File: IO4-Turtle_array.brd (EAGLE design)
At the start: 106 x 106 mm, 61 parts

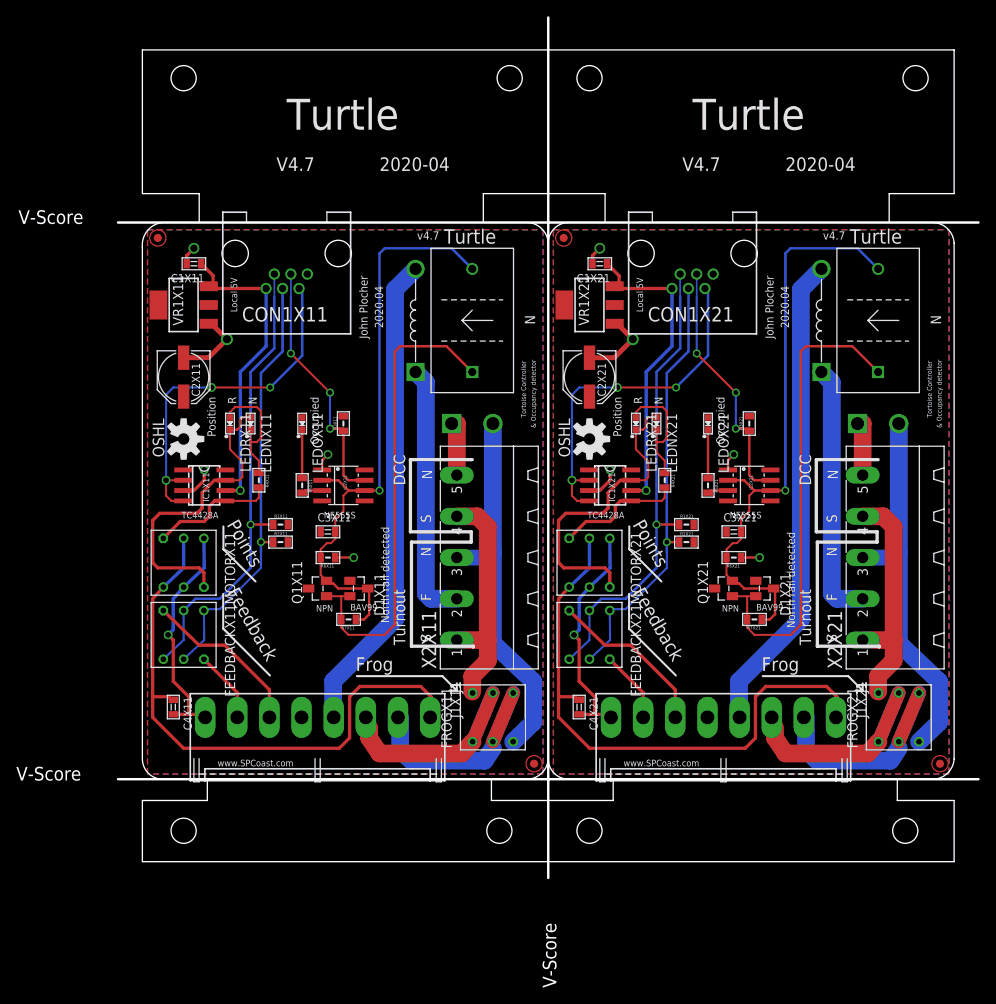
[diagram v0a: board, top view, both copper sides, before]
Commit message: silkscreen cleanup, better power routing
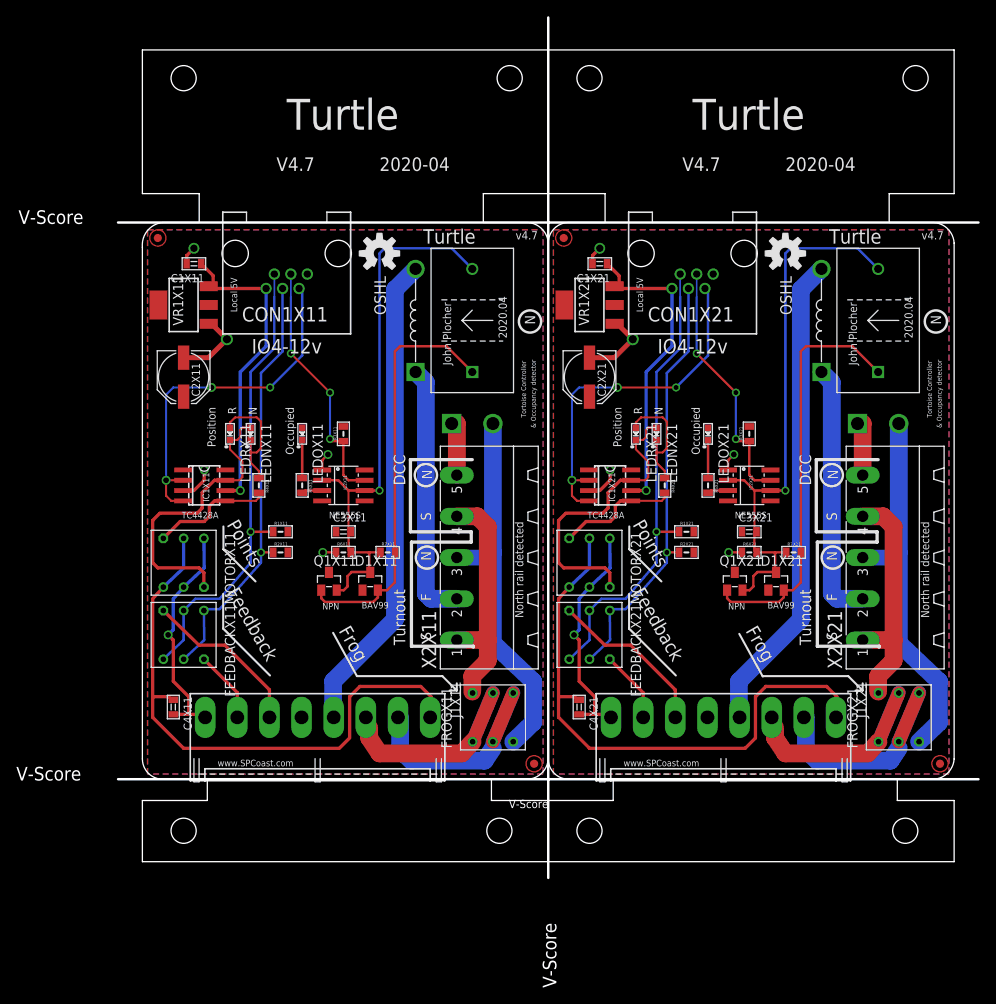
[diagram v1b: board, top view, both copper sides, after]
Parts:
- moved OSHW1X11 33.2 mm to (29.2, 74.9), turned to 0 degrees
- moved OSHW1X21 33.2 mm to (79.2, 74.9), turned to 0 degrees
- moved R7X11 9.56 mm to (30.2, 38.1), turned to 0 degrees
- moved R7X21 9.56 mm to (80.2, 38.1), turned to 0 degrees
- moved R6X11 2.01 mm to (24.8, 38.1), turned to 0 degrees
- moved R6X21 2.01 mm to (74.8, 38.1), turned to 0 degrees
- moved C3X11 1.91 mm to (24.8, 40.6)
- moved C3X21 1.91 mm to (74.8, 40.6)
- moved D1X11 1.66 mm to (28.1, 34.5), turned to 0 degrees
- moved Q1X11 1.66 mm to (23.0, 34.5), turned to 0 degrees
- moved D1X21 1.66 mm to (78.1, 34.5), turned to 0 degrees
- moved Q1X21 1.66 mm to (73.0, 34.5), turned to 0 degrees
- moved LEDNX11 1.27 mm to (13.3, 52.7)
- moved LEDNX21 1.27 mm to (63.3, 52.7)
- moved LEDOX11 1.27 mm to (19.7, 52.7)
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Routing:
- net N$2X11: track 59.0 -> 51.3 mm
- net N$2X21: track 59.0 -> 51.3 mm
- net TRIGGERX21: track 73.3 -> 70.2 mm
- net TRIGGERX11: track 73.3 -> 70.2 mm
- net N$8X21: track 5.97 -> 4.70 mm
- net N$8X11: track 5.97 -> 4.70 mm
- net N$1X11: track 38.4 -> 37.1 mm
- net N$1X21: track 38.4 -> 37.1 mm
- net N$19X21: track 15.8 -> 15.2 mm
- net N$19X11: track 15.8 -> 15.2 mm
- net GNDX11: track 20.4 -> 19.8 mm
- net N$3X11: track 15.5 -> 14.8 mm
- net N$3X21: track 15.5 -> 14.8 mm
- net GNDX21: track 20.4 -> 19.8 mm
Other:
- board text added: "IO4-12v"
- board text added: "V-Score"

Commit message: added values for connectors
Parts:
- CON1X11, CON1X21: value (none) -> RJ12/6
- J1X11, J1X21: value (none) -> 0.156
- LMP1X11, LMP1X21: value (none) -> 12v
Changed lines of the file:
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@@
 <setting verticaltext="up"/>
 </settings>
-<grid distance="50" unitdist="mil" unit="mil" style="dots" multiple="2" display="yes" altdistance="5" altunitdist="mil" altunit="mil"/>
+<grid distance="50" unitdist="mil" unit="mil" style="dots" multiple="2" display="yes" altdistance="25" altunitdist="mil" altunit="mil"/>
 <layers>
 <layer number="1" name="Top" color="4" fill="1" visible="yes" active="yes"/>
@@
 <element name="C3X11" library="SPCoast" package="0805-CAP" value="" x="24.765" y="40.64"/>
 <element name="C4X11" library="SPCoast" package="0805-CAP" value="" x="3.81" y="19.05" rot="R270"/>
-<element name="CON1X11" library="SPCoast" package="RJ25-INVERTED" value="" x="17.78" y="74.93" rot="R180"/>
+<element name="CON1X11" library="SPCoast" package="RJ25-INVERTED" value="RJ12/6" x="17.78" y="74.93" rot="R180"/>
 <element name="D1X11" library="SPCoast" package="SOT23" value="" x="28.067" y="34.544"/>
 <element name="FEEDBACKX11" library="SPCoast" package="8X8-SQ-PB" value="" x="5.08" y="27.94" rot="R270"/>
@@
 <element name="IC1X11" library="SPCoast" package="SO-08" value="" x="7.62" y="46.355" rot="R270"/>
 <element name="IC2X11" library="SPCoast" package="SO08" value="" x="24.765" y="46.355" rot="R270"/>
-<element name="J1X11" library="SPCoast" package="KK-156-8-F" value="" x="21.59" y="17.78" rot="R180"/>
+<element name="J1X11" library="SPCoast" package="KK-156-8-F" value="0.156" x="21.59" y="17.78" rot="R180"/>
 <element name="LEDNX11" library="SPCoast" package="0603-LED" value="" x="13.335" y="52.705" rot="R270"/>
 <element name="LEDOX11" library="SPCoast" package="0603-LED" value="" x="19.685" y="52.705" rot="R270"/>
 <element name="LEDRX11" library="SPCoast" package="0603-LED" value="" x="10.795" y="52.705" rot="R270"/>
-<element name="LMP1X11" library="SPCoast" package="BULB-3156" value="" x="33.655" y="66.675" rot="R90"/>
+<element name="LMP1X11" library="SPCoast" package="BULB-3156" value="12v" x="33.655" y="66.675" rot="R90"/>
 <element name="MOTORX11" library="SPCoast" package="8X8-SQ-PB" value="" x="5.08" y="36.83" rot="R270"/>
 <element name="OSHW1X11" library="SPCoast" package="OSHW-LOGO-M" value="" x="29.21" y="74.93"/>
@@
 <element name="C3X21" library="SPCoast" package="0805-CAP" value="" x="74.765" y="40.64"/>
 <element name="C4X21" library="SPCoast" package="0805-CAP" value="" x="53.81" y="19.05" rot="R270"/>
-<element name="CON1X21" library="SPCoast" package="RJ25-INVERTED" value="" x="67.78" y="74.93" rot="R180"/>
+<element name="CON1X21" library="SPCoast" package="RJ25-INVERTED" value="RJ12/6" x="67.78" y="74.93" rot="R180"/>
 <element name="D1X21" library="SPCoast" package="SOT23" value="" x="78.067" y="34.544"/>
 <element name="FEEDBACKX21" library="SPCoast" package="8X8-SQ-PB" value="" x="55.08" y="27.94" rot="R270"/>
@@
 <element name="IC1X21" library="SPCoast" package="SO-08" value="" x="57.62" y="46.355" rot="R270"/>
 <element name="IC2X21" library="SPCoast" package="SO08" value="" x="74.765" y="46.355" rot="R270"/>
-<element name="J1X21" library="SPCoast" package="KK-156-8-F" value="" x="71.59" y="17.78" rot="R180"/>
+<element name="J1X21" library="SPCoast" package="KK-156-8-F" value="0.156" x="71.59" y="17.78" rot="R180"/>
 <element name="LEDNX21" library="SPCoast" package="0603-LED" value="" x="63.335" y="52.705" rot="R270"/>
 <element name="LEDOX21" library="SPCoast" package="0603-LED" value="" x="69.685" y="52.705" rot="R270"/>
 <element name="LEDRX21" library="SPCoast" package="0603-LED" value="" x="60.795" y="52.705" rot="R270"/>
-<element name="LMP1X21" library="SPCoast" package="BULB-3156" value="" x="83.655" y="66.675" rot="R90"/>
+<element name="LMP1X21" library="SPCoast" package="BULB-3156" value="12v" x="83.655" y="66.675" rot="R90"/>
 <element name="MOTORX21" library="SPCoast" package="8X8-SQ-PB" value="" x="55.08" y="36.83" rot="R270"/>
 <element name="OSHW1X21" library="SPCoast" package="OSHW-LOGO-M" value="" x="79.21" y="74.93"/>

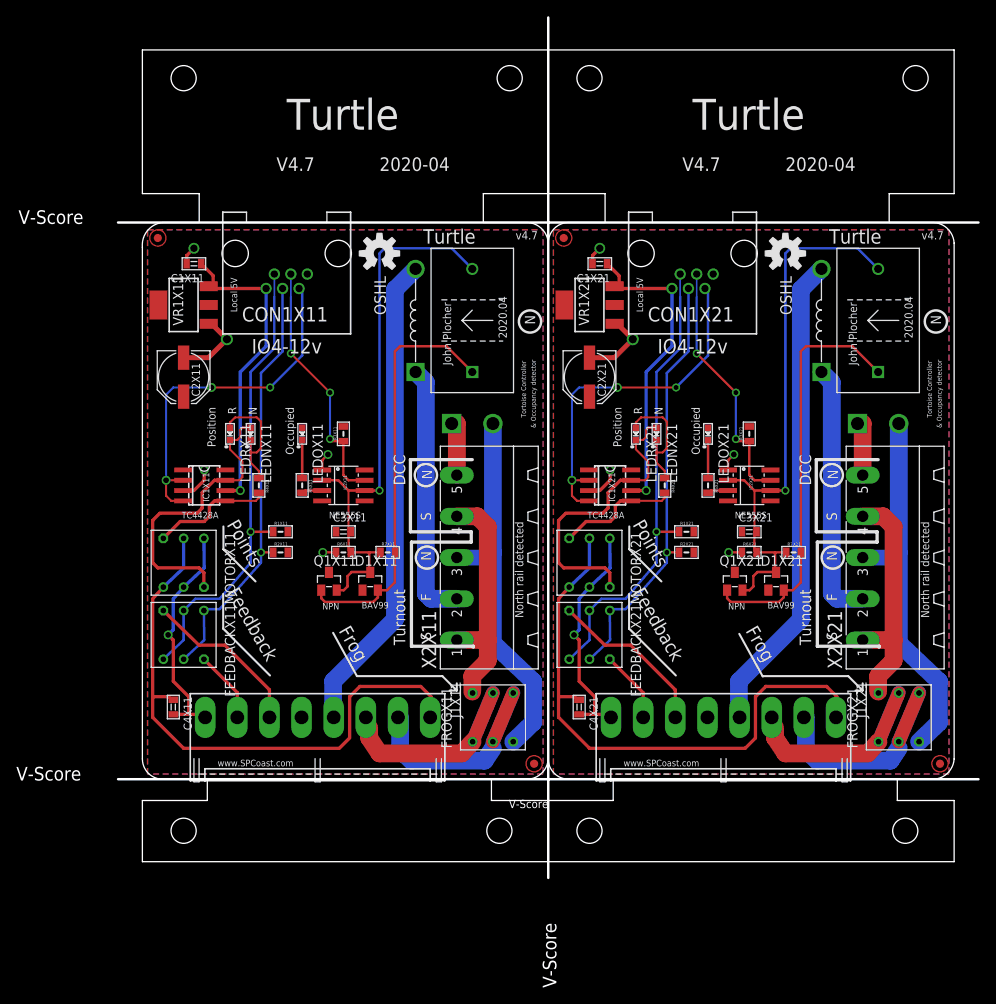
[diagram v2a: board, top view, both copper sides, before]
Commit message: added values for connectors
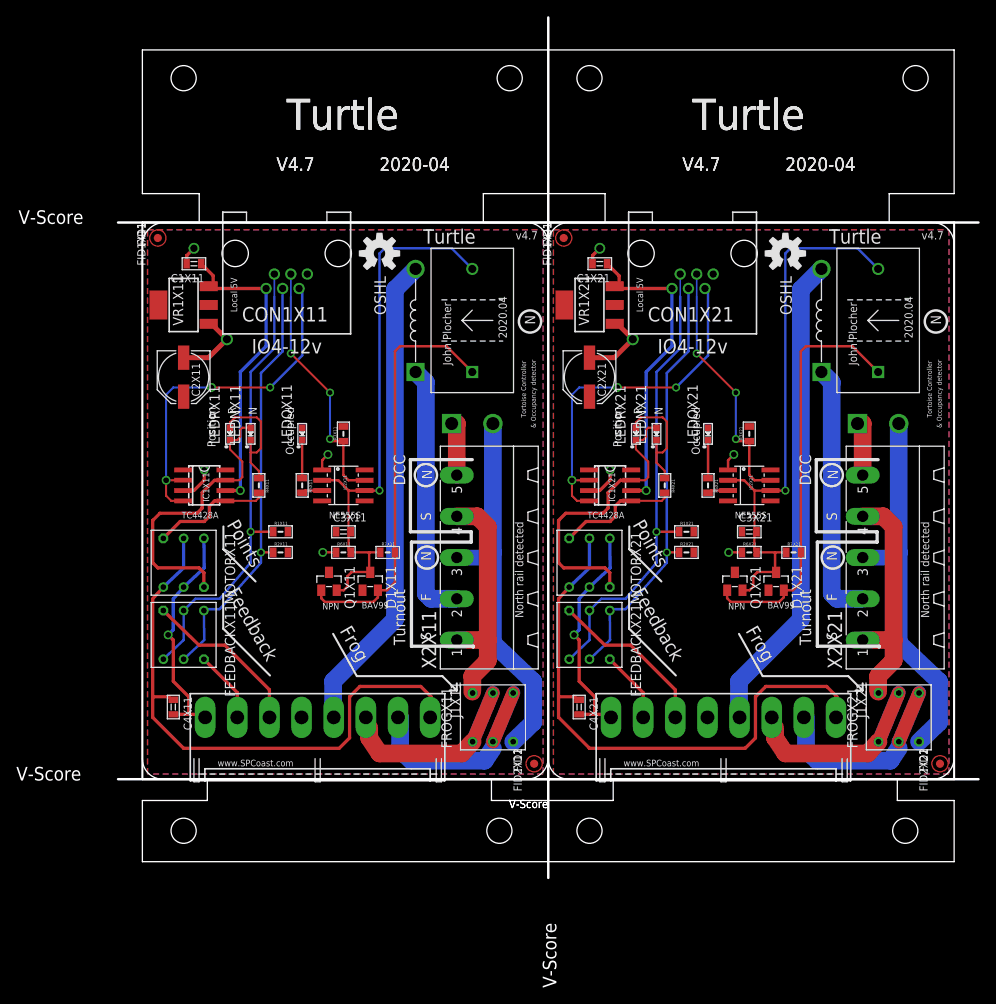
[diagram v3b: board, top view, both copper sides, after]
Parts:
- C1X11, C1X21: value (none) -> 10uf
- C2X11, C2X21: value (none) -> 100uf
- C3X11, C3X21: value (none) -> 2.2uf
- C4X11, C4X21: value (none) -> 0.1uf
- D1X11, D1X21: value (none) -> BAV99
- FEEDBACKX11, FEEDBACKX21, FROGX11, FROGX21, MOTORX11, MOTORX21: value (none) -> DPDT
- FID1X11, FID1X21, FID2X11, FID2X21: value (none) -> FIDUCIAL
- IC1X11, IC1X21: value (none) -> TC4428A
- IC2X11, IC2X21: value (none) -> NE555S
- LEDNX11, LEDNX21: value (none) -> G
- LEDOX11, LEDOX21: value (none) -> Y
- LEDRX11, LEDRX21: value (none) -> R
- OSHW1X11, OSHW1X21: value (none) -> DOC-OSHW-LOGO-M
- Q1X11, Q1X21: value (none) -> NPN
- R1X11, R1X21, R2X11, R2X21, R3X11, R3X21: value (none) -> 10k
- R4X11, R4X21: value (none) -> 2K0
- R5X11, R5X21: value (none) -> 1K0
- R6X11, R6X21: value (none) -> 1M0
- R7X11, R7X21: value (none) -> 10K
- TR1X11, TR1X21: value (none) -> CoilCraft
- VR1X11, VR1X21: value (none) -> LM1117-5
- X2X11, X2X21: value (none) -> MSTBA5
- turned D1X11 to 270 degrees
- turned D1X21 to 270 degrees
- turned Q1X11 to 270 degrees
- turned Q1X21 to 270 degrees
- turned LEDNX11 to 90 degrees
- turned LEDNX21 to 90 degrees
- turned LEDOX11 to 90 degrees
- turned LEDOX21 to 90 degrees
- turned LEDRX11 to 90 degrees
- turned LEDRX21 to 90 degrees
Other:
- board text added: "FID1"
- board text added: "FID2"

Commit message: added values for connectors
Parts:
- X2X1: value (none) -> 10x10
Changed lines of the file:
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@@
 <element name="VR1X21" library="SPCoast" package="SOT223" value="LM1117-5" x="55.08" y="68.58" rot="R90"/>
 <element name="X2X21" library="SPCoast" package="MSTBA5" value="MSTBA5" x="93.815" y="37.465" rot="R90"/>
-<element name="X2X1" library="SPCoast" package="BOARD-DINRAIL-2.7IN-5CM-DUAL" value="" x="0" y="0"/>
+<element name="X2X1" library="SPCoast" package="BOARD-DINRAIL-2.7IN-5CM-DUAL" value="10x10" x="0" y="0"/>
 </elements>
 <signals>

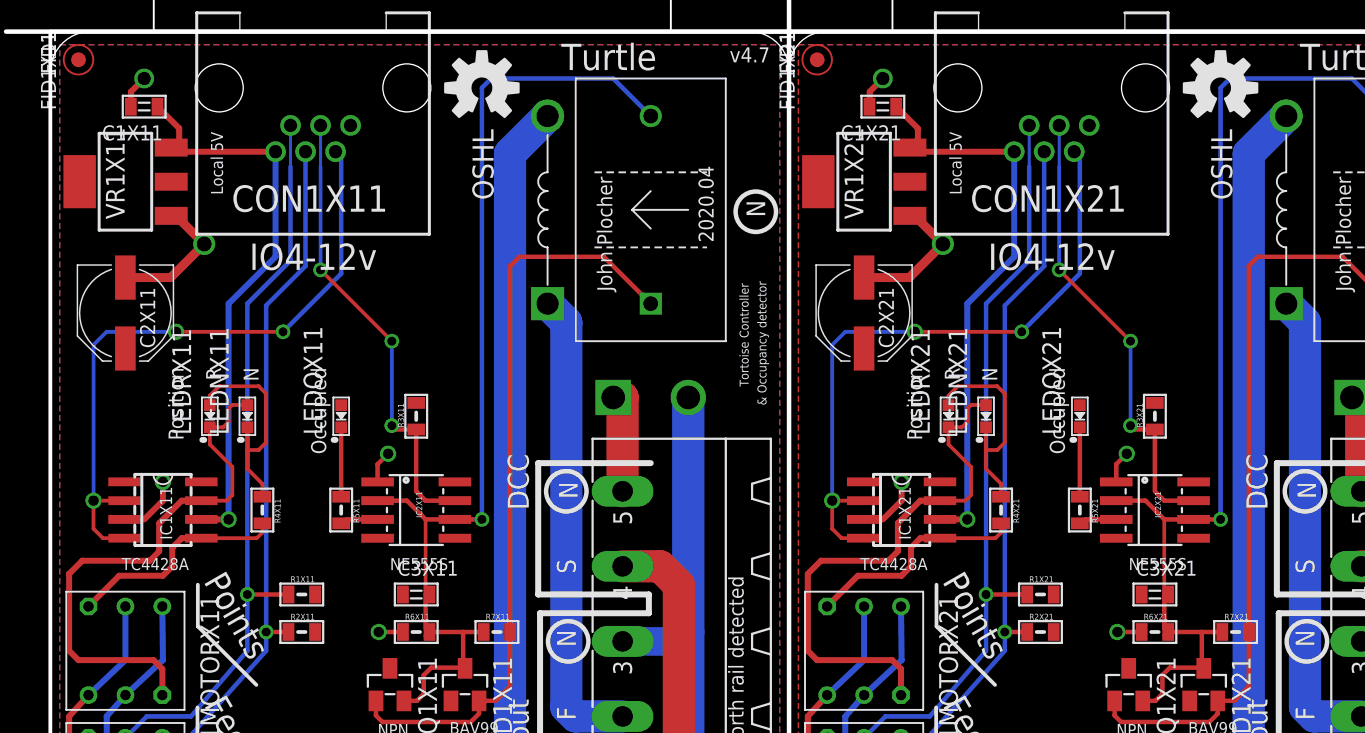
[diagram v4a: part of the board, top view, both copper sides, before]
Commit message: normalized values
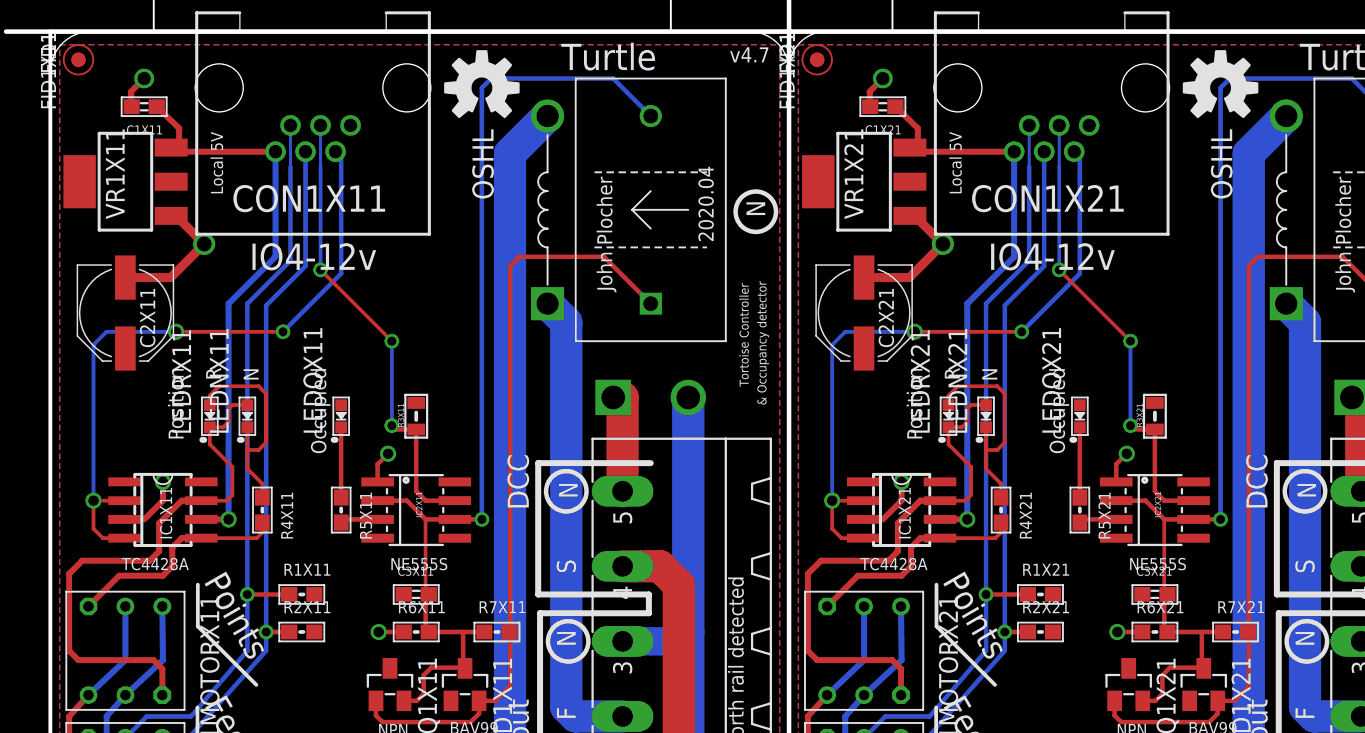
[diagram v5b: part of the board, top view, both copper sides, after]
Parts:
- C1X11, C1X21, C3X11, C3X21: device SPCoast:0805-CAP -> SPCoast:0603-CAP
- OSHW1X11, OSHW1X21: value DOC-OSHW-LOGO-M -> OSHW
- R1X11, R1X21, R2X11, R2X21, R4X11, R4X21, R5X11, R5X21, R6X11, R6X21, R7X11, R7X21: device SPCoast:0805-RES -> SPCoast:0603-RES
- X2X11, X2X21: value MSTBA5 -> 0.200
